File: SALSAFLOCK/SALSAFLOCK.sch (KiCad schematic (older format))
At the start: 14 parts, among them P1 INPUT, P2 ANTENNA, Q1 MOSFET_N

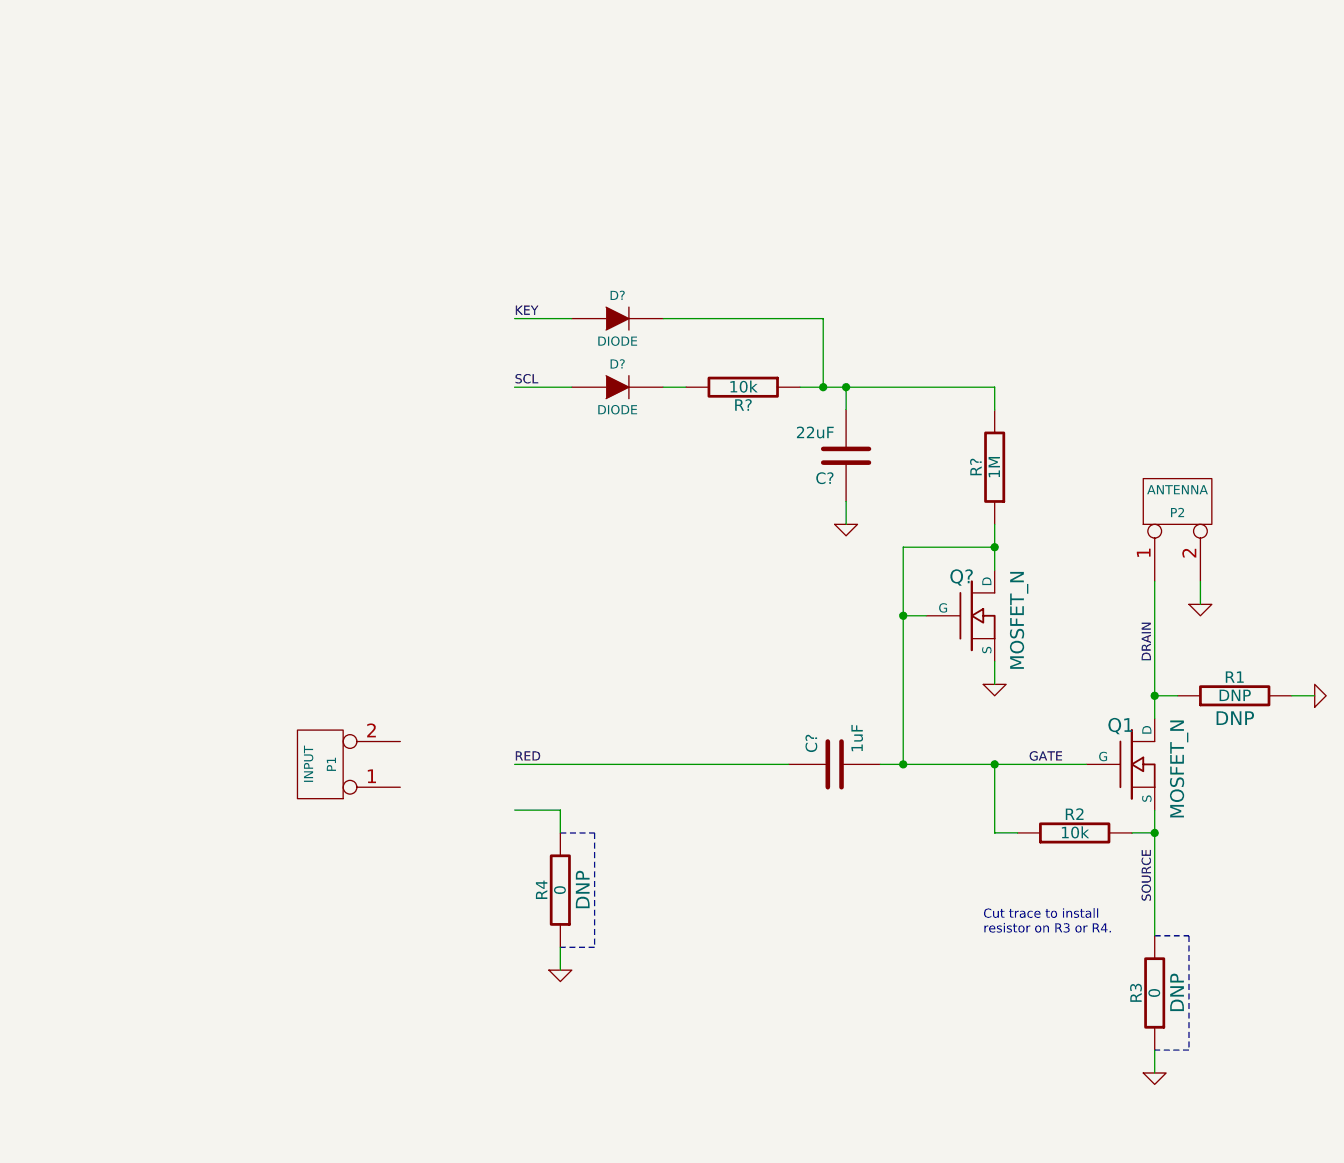
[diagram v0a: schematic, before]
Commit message: added VGA connectors
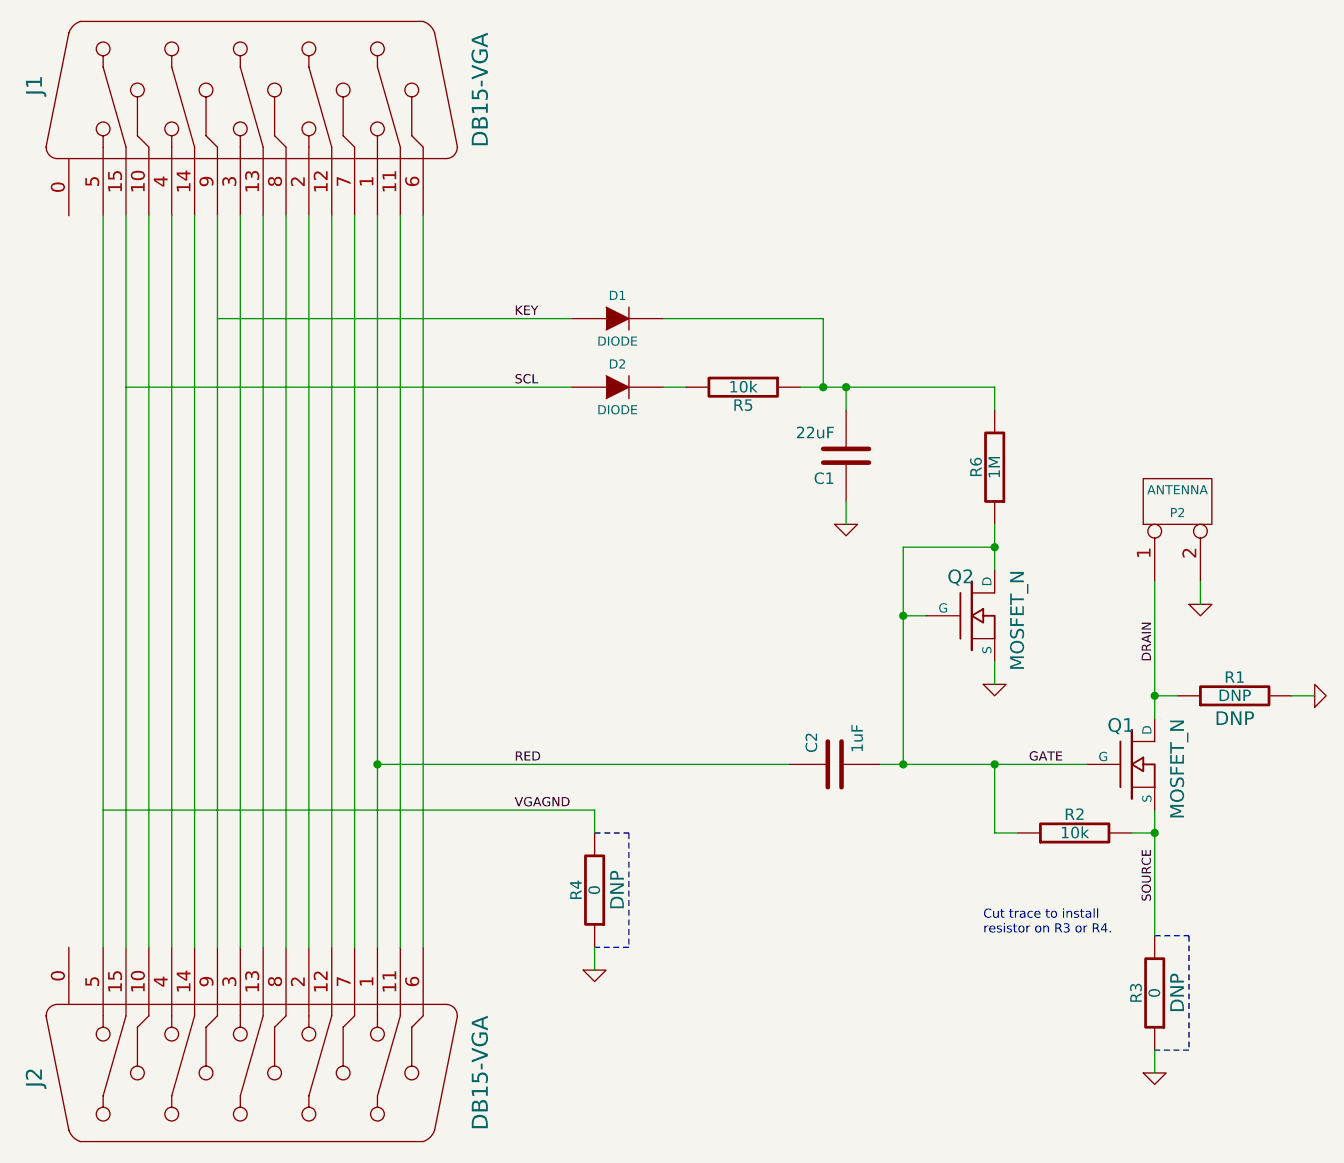
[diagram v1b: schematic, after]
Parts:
- removed P1: INPUT, symbol CONN_2
- added J1, J2: DB15-VGA, symbol DB15-VGA
- gave numbers to parts that had none: 7
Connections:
- net labels added: VGAGND
- wire segments 36 -> 52
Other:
- moved on the sheet: R4
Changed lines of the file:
@@
-EESchema Schematic File Version 2  date Wed 09 Jul 2014 12:39:05 PM MDT
+EESchema Schematic File Version 2  date Thu 17 Jul 2014 09:13:24 AM MDT
 LIBS:power
 LIBS:device
@@
 LIBS:contrib
 LIBS:valves
+LIBS:retroreflectors
 LIBS:SALSAFLOCK-cache
 EELAYER 27 0
@@
 Sheet 1 1
 Title ""
-Date "9 jul 2014"
+Date "17 jul 2014"
 Rev ""
 Comp ""
@@
 $EndComp
 $Comp
-L GND #PWR01
+L GND #PWR6
 U 1 1 5370DB21
 P 7300 5550
-F 0 "#PWR01" H 7300 5550 30  0001 C CNN
+F 0 "#PWR6" H 7300 5550 30  0001 C CNN
 F 1 "GND" H 7300 5480 30  0001 C CNN
 	1    7300 5550
@@
 $EndComp
 $Comp
-L GND #PWR02
+L GND #PWR4
 U 1 1 5370DB27
 P 8000 3900
-F 0 "#PWR02" H 8000 3900 30  0001 C CNN
+F 0 "#PWR4" H 8000 3900 30  0001 C CNN
 F 1 "GND" H 8000 3830 30  0001 C CNN
 	1    8000 3900
@@
 $EndComp
 $Comp
-L GND #PWR03
+L GND #PWR2
 U 1 1 53B0316B
 P 7500 3500
-F 0 "#PWR03" H 7500 3500 30  0001 C CNN
+F 0 "#PWR2" H 7500 3500 30  0001 C CNN
 F 1 "GND" H 7500 3430 30  0001 C CNN
 	1    7500 3500
@@
 $EndComp
 $Comp
-L CONN_2 P1
-U 1 1 53B03194
-P 3650 4200
-F 0 "P1" V 3600 4200 40  0000 C CNN
-F 1 "INPUT" V 3700 4200 40  0000 C CNN
-	1    3650 4200
-	-1   0    0    1
-$EndComp
-$Comp
-L GND #PWR04
+L GND #PWR5
 U 1 1 53B031B0
-P 4700 5100
-F 0 "#PWR04" H 4700 5100 30  0001 C CNN
-F 1 "GND" H 4700 5030 30  0001 C CNN
-	1    4700 5100
+P 4850 5100
+F 0 "#PWR5" H 4850 5100 30  0001 C CNN
+F 1 "GND" H 4850 5030 30  0001 C CNN
+	1    4850 5100
 	1    0    0    -1
 $EndComp
@@
 L R R4
 U 1 1 53B032AD
-P 4700 4750
-F 0 "R4" V 4780 4750 50  0000 C CNN
-F 1 "0" V 4700 4750 50  0000 C CNN
-F 4 "DNP" V 4600 4750 60  0000 C CNN "Note"
-	1    4700 4750
+P 4850 4750
+F 0 "R4" V 4930 4750 50  0000 C CNN
+F 1 "0" V 4850 4750 50  0000 C CNN
+F 4 "DNP" V 4750 4750 60  0000 C CNN "Note"
+	1    4850 4750
 	-1   0    0    1
 $EndComp
@@
 Cut trace to install\nresistor on R3 or R4.
 $Comp
-L MOSFET_N Q?
+L MOSFET_N Q2
 U 1 1 53BD8551
 P 6500 3550
-F 0 "Q?" H 6510 3720 60  0000 R CNN
+F 0 "Q2" H 6510 3720 60  0000 R CNN
 F 1 "MOSFET_N" V 6700 3750 60  0000 R CNN
 F 4 "Rohm Semiconductor" H 6500 3550 60  0001 C CNN "Manufacturer"
@@
 $EndComp
 $Comp
-L GND #PWR?
+L GND #PWR3
 U 1 1 53BD8575
 P 6600 3850
-F 0 "#PWR?" H 6600 3850 30  0001 C CNN
+F 0 "#PWR3" H 6600 3850 30  0001 C CNN
 F 1 "GND" H 6600 3780 30  0001 C CNN
 	1    6600 3850
@@
 $EndComp
 $Comp
-L R R?
+L R R5
 U 1 1 53BD859D
 P 5500 2550
-F 0 "R?" V 5580 2550 50  0000 C CNN
+F 0 "R5" V 5580 2550 50  0000 C CNN
 F 1 "10k" V 5500 2550 50  0000 C CNN
 	1    5500 2550
@@
 $EndComp
 $Comp
-L C C?
+L C C2
 U 1 1 53BD8613
 P 5900 4200
-F 0 "C?" H 5950 4300 50  0000 L CNN
+F 0 "C2" H 5950 4300 50  0000 L CNN
 F 1 "1uF" H 5950 4100 50  0000 L CNN
 	1    5900 4200
@@
 $EndComp
 $Comp
-L R R?
+L R R6
 U 1 1 53BD8718
 P 6600 2900
-F 0 "R?" V 6680 2900 50  0000 C CNN
+F 0 "R6" V 6680 2900 50  0000 C CNN
 F 1 "1M" V 6600 2900 50  0000 C CNN
 	1    6600 2900
@@
 $EndComp
 $Comp
-L C C?
+L C C1
 U 1 1 53BD8720
 P 5950 2850
-F 0 "C?" H 6000 2950 50  0000 L CNN
+F 0 "C1" H 6000 2950 50  0000 L CNN
 F 1 "22uF" H 6000 2750 50  0000 L CNN
 	1    5950 2850
@@
 $EndComp
 $Comp
-L DIODE D?
+L DIODE D2
 U 1 1 53BD8856
 P 4950 2550
-F 0 "D?" H 4950 2650 40  0000 C CNN
+F 0 "D2" H 4950 2650 40  0000 C CNN
 F 1 "DIODE" H 4950 2450 40  0000 C CNN
 	1    4950 2550
@@
 $EndComp
 $Comp
-L DIODE D?
+L DIODE D1
 U 1 1 53BD8992
 P 4950 2250
-F 0 "D?" H 4950 2350 40  0000 C CNN
+F 0 "D1" H 4950 2350 40  0000 C CNN
 F 1 "DIODE" H 4950 2150 40  0000 C CNN
 	1    4950 2250
@@
 $EndComp
 Wire Wire Line
-	6600 2550 5950 2550
-Wire Wire Line
-	5950 2550 5850 2550
-Wire Wire Line
-	5850 2550 5750 2550
-Wire Wire Line
-	5700 4200 4500 4200
+	5750 2550 5850 2550
+Wire Wire Line
+	5850 2550 5950 2550
+Wire Wire Line
+	5950 2550 6600 2550
 Wire Wire Line
 	6100 4200 6200 4200
@@
 	7300 4950 7450 4950
 Wire Notes Line
-	4850 5000 4700 5000
-Wire Notes Line
-	4850 4500 4850 5000
-Wire Notes Line
-	4700 4500 4850 4500
-Wire Wire Line
-	4700 5000 4700 5100
-Wire Wire Line
-	4700 4400 4700 4500
-Wire Wire Line
-	4500 4400 4700 4400
+	5000 5000 4850 5000
+Wire Notes Line
+	5000 4500 5000 5000
+Wire Notes Line
+	4850 4500 5000 4500
+Wire Wire Line
+	4850 5000 4850 5100
+Wire Wire Line
+	4850 4400 4850 4500
+Wire Wire Line
+	2700 4400 4850 4400
 Connection ~ 7300 4500
 Wire Wire Line
@@
 Connection ~ 5950 2550
 Wire Wire Line
-	4500 2250 4750 2250
-Wire Wire Line
-	4500 2550 4750 2550
-$Comp
-L GND #PWR?
+	3200 2250 4750 2250
+Wire Wire Line
+	2800 2550 4750 2550
+$Comp
+L GND #PWR1
 U 1 1 53BD8AD7
 P 5950 3150
-F 0 "#PWR?" H 5950 3150 30  0001 C CNN
+F 0 "#PWR1" H 5950 3150 30  0001 C CNN
 F 1 "GND" H 5950 3080 30  0001 C CNN
 	1    5950 3150
@@
 Wire Wire Line
 	7500 3400 7500 3500
+$Comp
+L DB15-VGA J1
+U 1 1 53C80301
+P 3300 1250
+F 0 "J1" H 3320 2150 70  0000 C CNN
+F 1 "DB15-VGA" H 3300 200 70  0000 C CNN
+	1    3300 1250
+	0    -1   -1   0
+$EndComp
+$Comp
+L DB15-VGA J2
+U 1 1 53C8030E
+P 3300 5550
+F 0 "J2" H 3320 6450 70  0000 C CNN
+F 1 "DB15-VGA" H 3300 4500 70  0000 C CNN
+	1    3300 5550
+	0    -1   1    0
+$EndComp
+Wire Wire Line
+	2700 1800 2700 5000
+Wire Wire Line
+	2800 1800 2800 5000
+Wire Wire Line
+	2900 1800 2900 5000
+Wire Wire Line
+	3000 1800 3000 5000
+Wire Wire Line
+	3100 1800 3100 5000
+Wire Wire Line
+	3200 1800 3200 5000
+Wire Wire Line
+	3300 1800 3300 5000
+Wire Wire Line
+	3400 1800 3400 5000
+Wire Wire Line
+	3500 1800 3500 5000
+Wire Wire Line
+	3600 1800 3600 5000
+Wire Wire Line
+	3700 1800 3700 5000
+Wire Wire Line
+	3800 1800 3800 5000
+Wire Wire Line
+	3900 1800 3900 4200
+Wire Wire Line
+	3900 4200 3900 5000
+Wire Wire Line
+	4000 1800 4000 5000
+Wire Wire Line
+	4100 1800 4100 5000
+Connection ~ 3900 4200
+Wire Wire Line
+	3900 4200 5700 4200
+Text Label 4500 4400 0    40   ~ 0
+VGAGND
 $EndSCHEMATC

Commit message: connector layout
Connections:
- net labels added: SHIELD
- wire segments 52 -> 44
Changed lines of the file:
@@
-EESchema Schematic File Version 2  date Thu 17 Jul 2014 09:13:24 AM MDT
+EESchema Schematic File Version 2  date Thu 17 Jul 2014 03:59:38 PM MDT
 LIBS:power
 LIBS:device
@@
 $EndComp
 $Comp
-L GND #PWR6
+L GND #PWR01
 U 1 1 5370DB21
 P 7300 5550
-F 0 "#PWR6" H 7300 5550 30  0001 C CNN
+F 0 "#PWR01" H 7300 5550 30  0001 C CNN
 F 1 "GND" H 7300 5480 30  0001 C CNN
 	1    7300 5550
@@
 $EndComp
 $Comp
-L GND #PWR4
+L GND #PWR02
 U 1 1 5370DB27
 P 8000 3900
-F 0 "#PWR4" H 8000 3900 30  0001 C CNN
+F 0 "#PWR02" H 8000 3900 30  0001 C CNN
 F 1 "GND" H 8000 3830 30  0001 C CNN
 	1    8000 3900
@@
 $EndComp
 $Comp
-L GND #PWR2
+L GND #PWR03
 U 1 1 53B0316B
 P 7500 3500
-F 0 "#PWR2" H 7500 3500 30  0001 C CNN
+F 0 "#PWR03" H 7500 3500 30  0001 C CNN
 F 1 "GND" H 7500 3430 30  0001 C CNN
 	1    7500 3500
@@
 $EndComp
 $Comp
-L GND #PWR5
+L GND #PWR04
 U 1 1 53B031B0
 P 4850 5100
-F 0 "#PWR5" H 4850 5100 30  0001 C CNN
+F 0 "#PWR04" H 4850 5100 30  0001 C CNN
 F 1 "GND" H 4850 5030 30  0001 C CNN
 	1    4850 5100
@@
 $EndComp
 $Comp
-L GND #PWR3
+L GND #PWR05
 U 1 1 53BD8575
 P 6600 3850
-F 0 "#PWR3" H 6600 3850 30  0001 C CNN
+F 0 "#PWR05" H 6600 3850 30  0001 C CNN
 F 1 "GND" H 6600 3780 30  0001 C CNN
 	1    6600 3850
@@
 $EndComp
 Wire Wire Line
-	5750 2550 5850 2550
-Wire Wire Line
-	5850 2550 5950 2550
-Wire Wire Line
-	5950 2550 6600 2550
-Wire Wire Line
-	6100 4200 6200 4200
-Wire Wire Line
-	6200 4200 6600 4200
-Wire Wire Line
-	6600 4200 7000 4200
+	5750 2550 6600 2550
+Wire Wire Line
+	6100 4200 7000 4200
 Connection ~ 6200 3550
 Connection ~ 6200 4200
@@
 	6600 3750 6600 3850
 Wire Wire Line
-	6600 3150 6600 3250
-Wire Wire Line
-	6600 3250 6600 3350
+	6600 3150 6600 3350
 Wire Wire Line
 	6200 3250 6600 3250
 Wire Wire Line
-	6200 3250 6200 3550
-Wire Wire Line
-	6200 3550 6200 4200
+	6200 3250 6200 4200
 Wire Wire Line
 	6300 3550 6200 3550
@@
 	7300 5550 7300 5450
 Wire Wire Line
-	7300 4400 7300 4500
-Wire Wire Line
-	7300 4500 7300 4950
+	7300 4400 7300 4950
 Connection ~ 7300 3900
 Wire Wire Line
@@
 Connection ~ 6600 4200
 Wire Wire Line
-	7300 3400 7300 3900
-Wire Wire Line
-	7300 3900 7300 4000
+	7300 3400 7300 4000
 Wire Wire Line
 	5850 2550 5850 2250
@@
 	2800 2550 4750 2550
 $Comp
-L GND #PWR1
+L GND #PWR06
 U 1 1 53BD8AD7
 P 5950 3150
-F 0 "#PWR1" H 5950 3150 30  0001 C CNN
+F 0 "#PWR06" H 5950 3150 30  0001 C CNN
 F 1 "GND" H 5950 3080 30  0001 C CNN
 	1    5950 3150
@@
 	3800 1800 3800 5000
 Wire Wire Line
-	3900 1800 3900 4200
-Wire Wire Line
-	3900 4200 3900 5000
+	3900 1800 3900 5000
 Wire Wire Line
 	4000 1800 4000 5000
@@
 Text Label 4500 4400 0    40   ~ 0
 VGAGND
+Wire Wire Line
+	2550 5000 2550 1800
+Connection ~ 3200 2250
+Connection ~ 2800 2550
+Connection ~ 2700 4400
+Text Label 2550 3450 1    40   ~ 0
+SHIELD
 $EndSCHEMATC

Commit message: finished SALSAFLOCK
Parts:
- removed D1, D2: DIODE, symbol DIODE
- added D1, D2: DIODE-SOT23-3, symbol DIODE-SOT23-3
- Q1, Q2: Description MOSFET N-CH 20V 300MA EMT3 -> MOSFET N-CH 10V 50MA SOT-143B; Manufacturer Rohm Semiconductor -> NXP; Part Number RUE003N02TL -> BSS83,215
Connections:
- net KEY: now also D1.1 (A)
- net SCL: now also D2.1 (A)
- net at C1.2, R5.1, R6.2: now also D1.3 (K)
- net at R5.2: now also D2.3 (K)
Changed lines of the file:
@@
-EESchema Schematic File Version 2  date Thu 17 Jul 2014 03:59:38 PM MDT
+EESchema Schematic File Version 2  date Sun 27 Jul 2014 09:41:48 PM MDT
 LIBS:power
 LIBS:device
@@
 Sheet 1 1
 Title ""
-Date "17 jul 2014"
+Date "28 jul 2014"
 Rev ""
 Comp ""
@@
 Comment4 ""
 $EndDescr
-$Comp
-L MOSFET_N Q1
-U 1 1 5370319E
-P 7200 4200
-F 0 "Q1" H 7210 4370 60  0000 R CNN
-F 1 "MOSFET_N" V 7400 4400 60  0000 R CNN
-F 4 "Rohm Semiconductor" H 7200 4200 60  0001 C CNN "Manufacturer"
-F 5 "RUE003N02TL" H 7200 4200 60  0001 C CNN "Part Number"
-F 6 "MOSFET N-CH 20V 300MA EMT3" H 7200 4200 60  0001 C CNN "Description"
-	1    7200 4200
-	1    0    0    -1
-$EndComp
 $Comp
 L R R2
@@
 $EndComp
 $Comp
-L GND #PWR01
+L GND #PWR6
 U 1 1 5370DB21
 P 7300 5550
-F 0 "#PWR01" H 7300 5550 30  0001 C CNN
+F 0 "#PWR6" H 7300 5550 30  0001 C CNN
 F 1 "GND" H 7300 5480 30  0001 C CNN
 	1    7300 5550
@@
 $EndComp
 $Comp
-L GND #PWR02
+L GND #PWR4
 U 1 1 5370DB27
 P 8000 3900
-F 0 "#PWR02" H 8000 3900 30  0001 C CNN
+F 0 "#PWR4" H 8000 3900 30  0001 C CNN
 F 1 "GND" H 8000 3830 30  0001 C CNN
 	1    8000 3900
@@
 $EndComp
 $Comp
-L GND #PWR03
+L GND #PWR2
 U 1 1 53B0316B
 P 7500 3500
-F 0 "#PWR03" H 7500 3500 30  0001 C CNN
+F 0 "#PWR2" H 7500 3500 30  0001 C CNN
 F 1 "GND" H 7500 3430 30  0001 C CNN
 	1    7500 3500
@@
 $EndComp
 $Comp
-L GND #PWR04
+L GND #PWR5
 U 1 1 53B031B0
 P 4850 5100
-F 0 "#PWR04" H 4850 5100 30  0001 C CNN
+F 0 "#PWR5" H 4850 5100 30  0001 C CNN
 F 1 "GND" H 4850 5030 30  0001 C CNN
 	1    4850 5100
@@
 F 0 "Q2" H 6510 3720 60  0000 R CNN
 F 1 "MOSFET_N" V 6700 3750 60  0000 R CNN
-F 4 "Rohm Semiconductor" H 6500 3550 60  0001 C CNN "Manufacturer"
-F 5 "RUE003N02TL" H 6500 3550 60  0001 C CNN "Part Number"
-F 6 "MOSFET N-CH 20V 300MA EMT3" H 6500 3550 60  0001 C CNN "Description"
+F 4 "NXP" H 6500 3550 60  0001 C CNN "Manufacturer"
+F 5 "BSS83,215" H 6500 3550 60  0001 C CNN "Part Number"
+F 6 "MOSFET N-CH 10V 50MA SOT-143B" H 6500 3550 60  0001 C CNN "Description"
 	1    6500 3550
 	1    0    0    -1
 $EndComp
 $Comp
-L GND #PWR05
+L GND #PWR3
 U 1 1 53BD8575
 P 6600 3850
-F 0 "#PWR05" H 6600 3850 30  0001 C CNN
+F 0 "#PWR3" H 6600 3850 30  0001 C CNN
 F 1 "GND" H 6600 3780 30  0001 C CNN
 	1    6600 3850
@@
 	-1   0    0    1
 $EndComp
-$Comp
-L DIODE D2
-U 1 1 53BD8856
-P 4950 2550
-F 0 "D2" H 4950 2650 40  0000 C CNN
-F 1 "DIODE" H 4950 2450 40  0000 C CNN
-	1    4950 2550
-	1    0    0    -1
-$EndComp
-$Comp
-L DIODE D1
-U 1 1 53BD8992
-P 4950 2250
-F 0 "D1" H 4950 2350 40  0000 C CNN
-F 1 "DIODE" H 4950 2150 40  0000 C CNN
-	1    4950 2250
-	1    0    0    -1
-$EndComp
 Wire Wire Line
 	5750 2550 6600 2550
@@
 	2800 2550 4750 2550
 $Comp
-L GND #PWR06
+L GND #PWR1
 U 1 1 53BD8AD7
 P 5950 3150
-F 0 "#PWR06" H 5950 3150 30  0001 C CNN
+F 0 "#PWR1" H 5950 3150 30  0001 C CNN
 F 1 "GND" H 5950 3080 30  0001 C CNN
 	1    5950 3150
@@
 Text Label 2550 3450 1    40   ~ 0
 SHIELD
+$Comp
+L DIODE-SOT23-3 D1
+U 1 1 53D5C022
+P 4950 2250
+F 0 "D1" H 4950 2350 40  0000 C CNN
+F 1 "DIODE-SOT23-3" H 4950 2150 40  0000 C CNN
+F 4 "Fairchild" H 4950 2250 60  0001 C CNN "Manufacturer"
+F 5 "BAT54" H 4950 2250 60  0001 C CNN "Part Number"
+F 6 "DIODE SCHOTTKY 30V 0.2A SOT23-3" H 4950 2250 60  0001 C CNN "Description"
+	1    4950 2250
+	1    0    0    -1
+$EndComp
+$Comp
+L DIODE-SOT23-3 D2
+U 1 1 53D5C057
+P 4950 2550
+F 0 "D2" H 4950 2650 40  0000 C CNN
+F 1 "DIODE-SOT23-3" H 4950 2450 40  0000 C CNN
+F 4 "Fairchild" H 4950 2550 60  0001 C CNN "Manufacturer"
+F 5 "BAT54" H 4950 2550 60  0001 C CNN "Part Number"
+F 6 "DIODE SCHOTTKY 30V 0.2A SOT23-3" H 4950 2550 60  0001 C CNN "Description"
+	1    4950 2550
+	1    0    0    -1
+$EndComp
+$Comp
+L MOSFET_N Q1
+U 1 1 53D5C0DC
+P 7200 4200
+F 0 "Q1" H 7210 4370 60  0000 R CNN
+F 1 "MOSFET_N" V 7400 4400 60  0000 R CNN
+F 4 "NXP" H 7200 4200 60  0001 C CNN "Manufacturer"
+F 5 "BSS83,215" H 7200 4200 60  0001 C CNN "Part Number"
+F 6 "MOSFET N-CH 10V 50MA SOT-143B" H 7200 4200 60  0001 C CNN "Description"
+	1    7200 4200
+	1    0    0    -1
+$EndComp
 $EndSCHEMATC

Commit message: connected BSS83,215 substrate to source (previous workaround was solder blob)
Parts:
- Q1, Q2: symbol MOSFET_N -> MOS_N4
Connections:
- net GND: now also Q2.B
- net SOURCE: now also Q1.B
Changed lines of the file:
@@
-EESchema Schematic File Version 2  date Sun 27 Jul 2014 09:41:48 PM MDT
+EESchema Schematic File Version 2  date Tue 12 Aug 2014 10:44:59 PM MDT
 LIBS:power
 LIBS:device
@@
 Sheet 1 1
 Title ""
-Date "28 jul 2014"
+Date "13 aug 2014"
 Rev ""
 Comp ""
@@
 Text Label 6750 4200 0    40   ~ 0
 GATE
-Text Label 7300 4800 1    40   ~ 0
+Text Label 7300 4900 1    40   ~ 0
 SOURCE
 Text Notes 6550 4950 0    40   ~ 0
 Cut trace to install\nresistor on R3 or R4.
 $Comp
-L MOSFET_N Q2
+L MOS_N4 Q2
 U 1 1 53BD8551
 P 6500 3550
@@
 L GND #PWR3
 U 1 1 53BD8575
-P 6600 3850
-F 0 "#PWR3" H 6600 3850 30  0001 C CNN
-F 1 "GND" H 6600 3780 30  0001 C CNN
-	1    6600 3850
+P 6600 3950
+F 0 "#PWR3" H 6600 3950 30  0001 C CNN
+F 1 "GND" H 6600 3880 30  0001 C CNN
+	1    6600 3950
 	1    0    0    -1
 $EndComp
@@
 Connection ~ 6600 3250
 Wire Wire Line
-	6600 3750 6600 3850
+	6600 3750 6600 3950
 Wire Wire Line
 	6600 3150 6600 3350
@@
 $EndComp
 $Comp
-L MOSFET_N Q1
+L MOS_N4 Q1
 U 1 1 53D5C0DC
 P 7200 4200
@@
 	1    0    0    -1
 $EndComp
+Wire Wire Line
+	6650 3550 6750 3550
+Wire Wire Line
+	6750 3550 6750 3850
+Wire Wire Line
+	6750 3850 6600 3850
+Connection ~ 6600 3850
+Wire Wire Line
+	7350 4200 7450 4200
+Wire Wire Line
+	7450 4200 7450 4600
+Wire Wire Line
+	7450 4600 7300 4600
+Connection ~ 7300 4600
 $EndSCHEMATC

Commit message: changed R6 to 10k
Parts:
- R6: value 1M -> 10k
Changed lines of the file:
@@
-EESchema Schematic File Version 2  date Tue 12 Aug 2014 10:44:59 PM MDT
+EESchema Schematic File Version 2  date Tue 12 Aug 2014 10:48:10 PM MDT
 LIBS:power
 LIBS:device
@@
 P 6600 2900
 F 0 "R6" V 6680 2900 50  0000 C CNN
-F 1 "1M" V 6600 2900 50  0000 C CNN
+F 1 "10k" V 6600 2900 50  0000 C CNN
 	1    6600 2900
 	-1   0    0    1
